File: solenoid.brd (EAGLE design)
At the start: 35.6 x 30.5 mm, 41 parts, among them Y1 ECS-80-S-4X

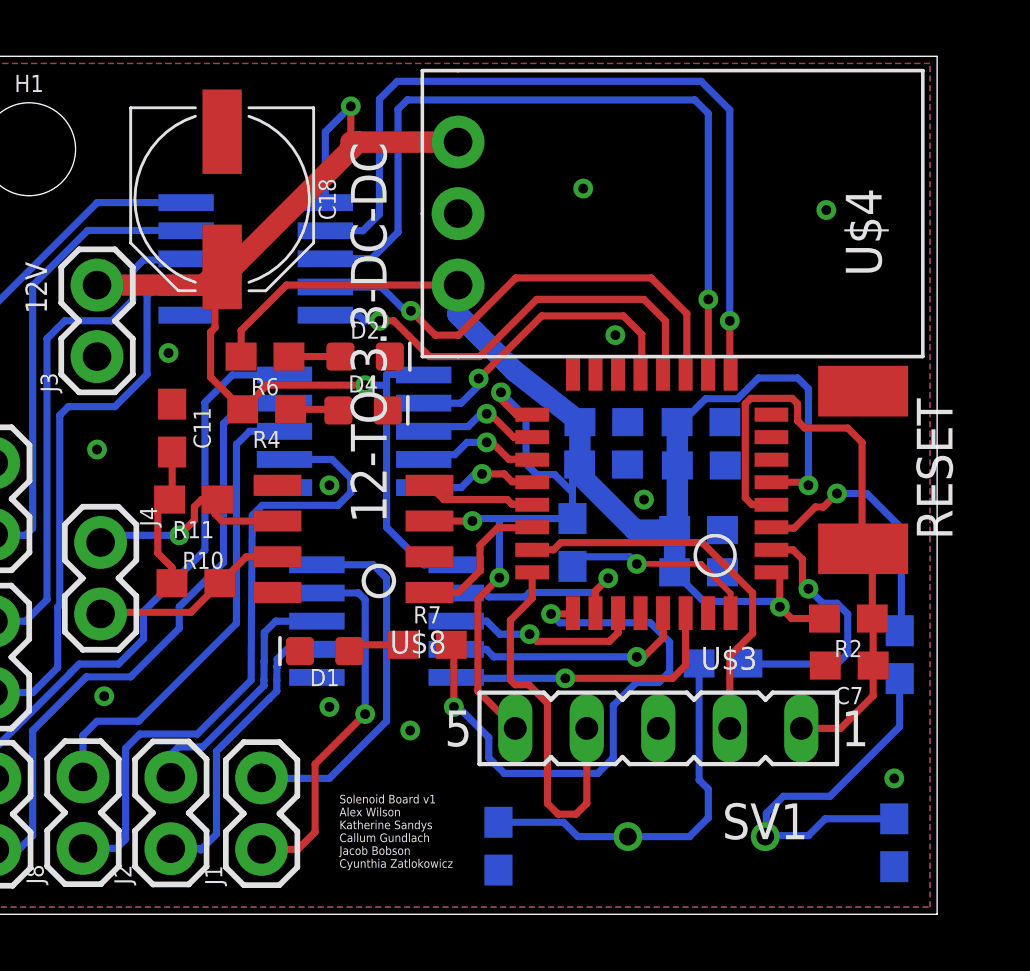
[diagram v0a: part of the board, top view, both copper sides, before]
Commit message: Update 12->3.3 converter, make extra layers inactive, fix names
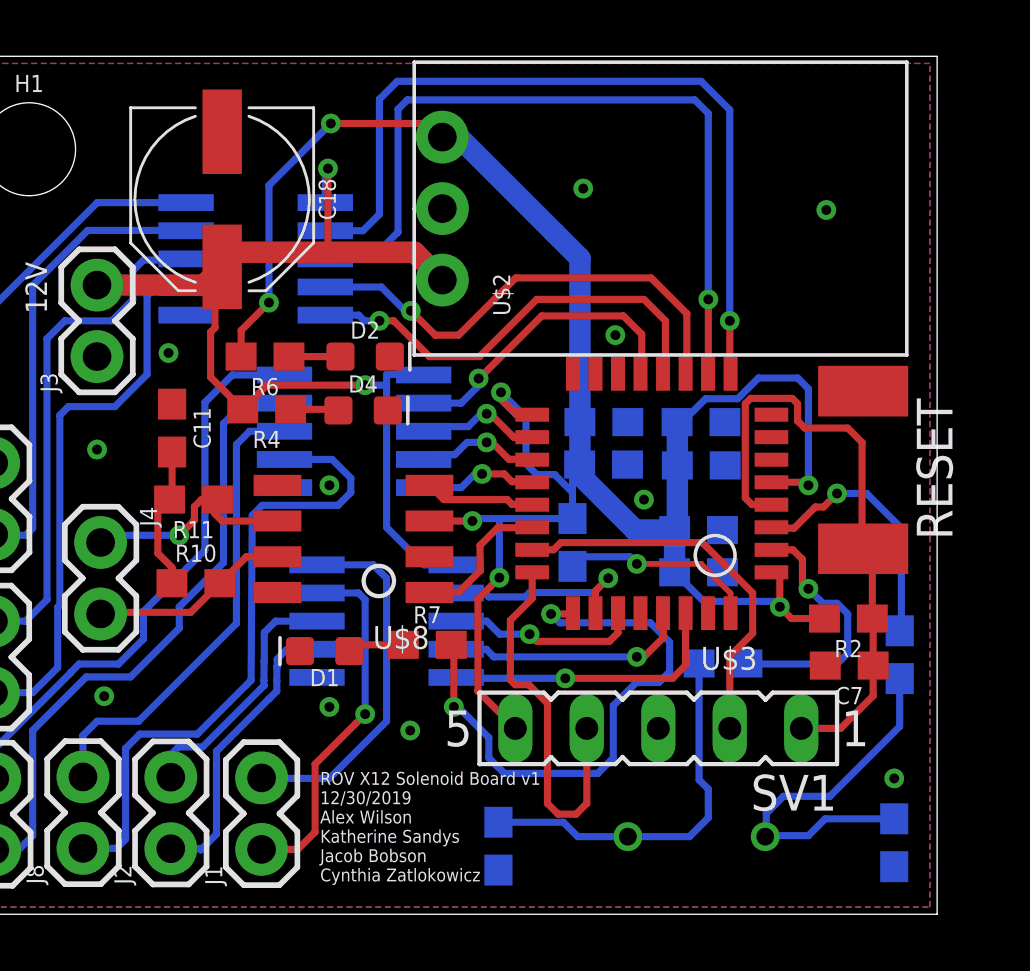
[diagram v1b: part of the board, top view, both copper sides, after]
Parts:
- removed U$4: 12-TO-3.3-DC-DC, ece477:MURATA-DCDC
- added U$2: MURATA-DC-DC, MURATA_3pin_dcdc:MURATA-DC-DC
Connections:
- net +3V3: now also U$2.3; no longer U$4.3.3V
- net 12V: now also U$2.1; no longer U$4.VIN
- net GND: now also U$2.2; no longer U$4.GND
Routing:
- net +3V3: track 67.5 -> 77.6 mm, vias 5 -> 7
- net 12V: track 41.1 -> 38.2 mm
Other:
- board text added: "ROV X12 Solenoid Board v1 12/30/2019 Alex Wilson Katherine Sandys Jacob Bobson Cynthia Zatlokowicz"
- board text removed: "Solenoid Board v1 Alex Wilson Katherine Sandys Callum Gundlach Jacob Bobson Cyunthia Zatlokowicz"

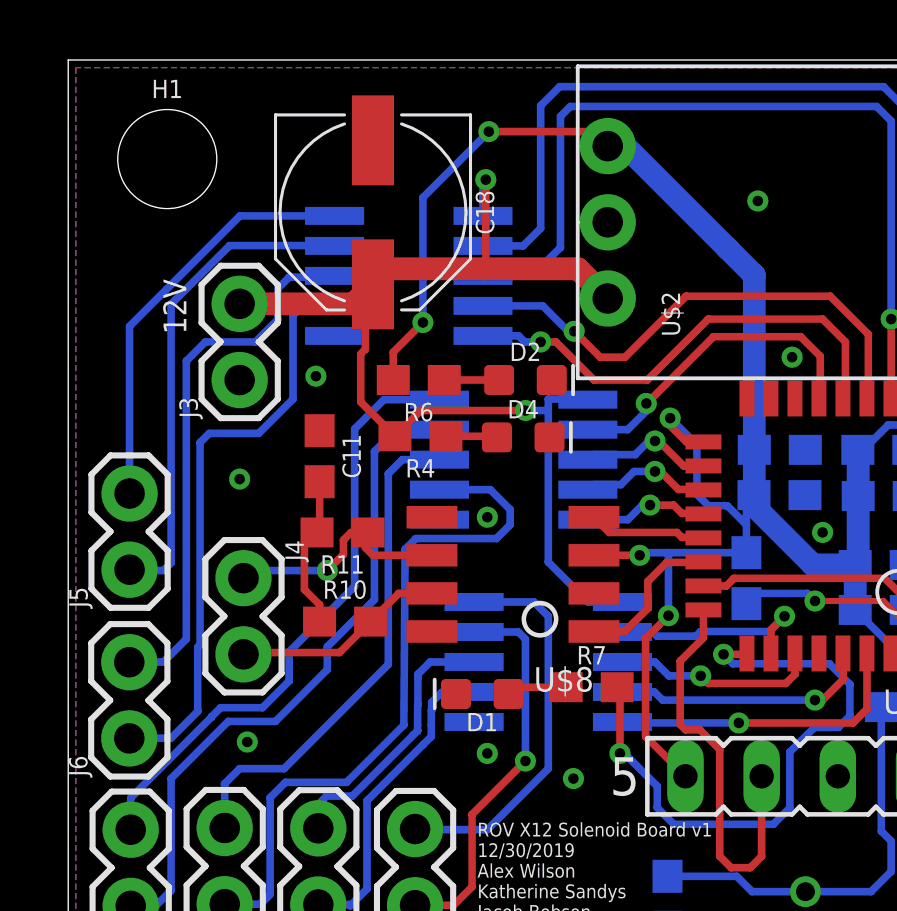
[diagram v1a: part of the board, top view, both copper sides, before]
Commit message: deleted h bridges - broken
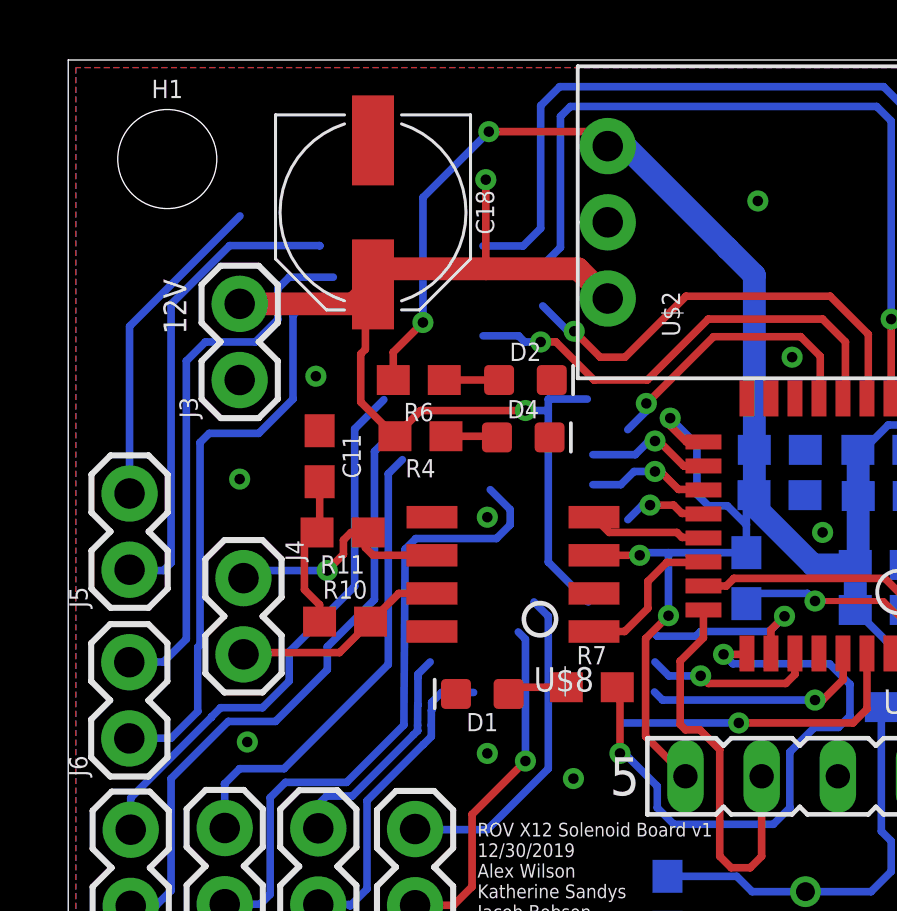
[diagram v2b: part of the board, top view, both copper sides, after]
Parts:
- removed U$1, U$5, U$6: LV8548M, HBridge:SOP100P600X175-10N
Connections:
- net 12V: no longer U$1.VCC, U$5.VCC, U$6.VCC
- net GND: no longer U$1.GND, U$5.GND, U$6.GND
- net GPIO0: no longer U$1.IN4
- net GPIO1: no longer U$1.IN3
- net GPIO10: no longer U$5.IN3
- net GPIO11: no longer U$5.IN4
- net GPIO12: no longer U$6.IN1
- net GPIO13: no longer U$6.IN2
- net GPIO14: no longer U$6.IN3
- net GPIO15: no longer U$6.IN4
- net GPIO2: no longer U$1.IN2
- net GPIO3: no longer U$1.IN1
- net GPIO8: no longer U$5.IN1
- net GPIO9: no longer U$5.IN2
- net SOL1_1: no longer U$1.OUT1
- net SOL1_2: no longer U$1.OUT2
- net SOL2_1: no longer U$1.OUT3
- net SOL2_2: no longer U$1.OUT4
- net SOL3_1: no longer U$5.OUT1
- net SOL3_2: no longer U$5.OUT2
- net SOL4_1: no longer U$5.OUT3
- net SOL4_2: no longer U$5.OUT4
- net SOL5_1: no longer U$6.OUT1
- net SOL5_2: no longer U$6.OUT2
- net SOL6_1: no longer U$6.OUT3
- net SOL6_2: no longer U$6.OUT4
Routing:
- net SOL3_1: track 13.9 -> 10.8 mm
- net 12V: track 38.2 -> 36.0 mm
- net SOL1_1: track 13.0 -> 11.0 mm
- net GPIO10: track 17.1 -> 15.1 mm
- net SOL5_1: track 20.5 -> 18.6 mm
- net SOL6_2: track 23.2 -> 21.5 mm
- net SOL1_2: track 13.0 -> 11.5 mm
- net SOL2_1: track 9.05 -> 7.59 mm
- net SOL5_2: track 22.4 -> 21.0 mm
- net GPIO15: track 4.18 -> 2.84 mm
- net GPIO12: track 10.9 -> 9.54 mm
- net SOL6_1: track 16.8 -> 15.6 mm
- net GPIO2: track 6.87 -> 5.79 mm
- net GPIO1: track 8.62 -> 7.56 mm
- net GPIO3: track 7.16 -> 6.14 mm

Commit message: owo
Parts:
- added U1, U2, U3, U4, U5, U6: QS5K2TR, QS5K2TR:SOT95P280X100-5N
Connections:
- net 12V: now also U1.2, U2.2, U3.2, U4.2, U5.2, U6.2
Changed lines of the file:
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@@
 <attribute name="VALUE" x="21.2852" y="21.2598" size="0.6096" layer="27" font="vector" ratio="20" rot="R90"/>
+</element>
+<element name="U1" library="QS5K2TR" package="SOT95P280X100-5N" value="QS5K2TR" x="-2.3622" y="0.635" smashed="yes">
+<attribute name="AVAILABILITY" value="Good" x="-2.3622" y="0.635" size="1.778" layer="27" display="off"/>
+<attribute name="DESCRIPTION" value=" Mosfet Array 2 N-Channel (Dual) Common Source 30V 2A 1.25W Surface Mount TSMT5 " x="-2.3622" y="0.635" size="1.778" layer="27" display="off"/>
+<attribute name="DIGIKEY-PURCHASE-URL" value="https://snapeda.com/shop?store=DigiKey&amp;id=623744" x="-2.3622" y="0.635" size="1.778" layer="27" display="off"/>
+<attribute name="MF" value="Rohm" x="-2.3622" y="0.635" size="1.778" layer="27" display="off"/>
+<attribute name="MOUSER-PURCHASE-URL" value="https://snapeda.com/shop?store=Mouser&amp;id=623744" x="-2.3622" y="0.635" size="1.778" layer="27" display="off"/>
+<attribute name="MP" value="QS5K2TR" x="-2.3622" y="0.635" size="1.778" layer="27" display="off"/>
+<attribute name="NAME" x="-3.46301875" y="2.436340625" size="0.406703125" layer="25"/>
+<attribute name="PACKAGE" value="SOT-23-5 Rohm" x="-2.3622" y="0.635" size="1.778" layer="27" display="off"/>
+<attribute name="PRICE" value="None" x="-2.3622" y="0.635" size="1.778" layer="27" display="off"/>
+<attribute name="VALUE" x="-3.462309375" y="-1.565209375" size="0.4064375" layer="27"/>
+</element>
+<element name="U2" library="QS5K2TR" package="SOT95P280X100-5N" value="QS5K2TR" x="-7.1628" y="0.635" smashed="yes">
+<attribute name="AVAILABILITY" value="Good" x="-7.1628" y="0.635" size="1.778" layer="27" display="off"/>
+<attribute name="DESCRIPTION" value=" Mosfet Array 2 N-Channel (Dual) Common Source 30V 2A 1.25W Surface Mount TSMT5 " x="-7.1628" y="0.635" size="1.778" layer="27" display="off"/>
+<attribute name="DIGIKEY-PURCHASE-URL" value="https://snapeda.com/shop?store=DigiKey&amp;id=623744" x="-7.1628" y="0.635" size="1.778" layer="27" display="off"/>
+<attribute name="MF" value="Rohm" x="-7.1628" y="0.635" size="1.778" layer="27" display="off"/>
+<attribute name="MOUSER-PURCHASE-URL" value="https://snapeda.com/shop?store=Mouser&amp;id=623744" x="-7.1628" y="0.635" size="1.778" layer="27" display="off"/>
+<attribute name="MP" value="QS5K2TR" x="-7.1628" y="0.635" size="1.778" layer="27" display="off"/>
+<attribute name="NAME" x="-8.26361875" y="2.436340625" size="0.406703125" layer="25"/>
+<attribute name="PACKAGE" value="SOT-23-5 Rohm" x="-7.1628" y="0.635" size="1.778" layer="27" display="off"/>
+<attribute name="PRICE" value="None" x="-7.1628" y="0.635" size="1.778" layer="27" display="off"/>
+<attribute name="VALUE" x="-8.262909375" y="-1.565209375" size="0.4064375" layer="27"/>
+</element>
+<element name="U3" library="QS5K2TR" package="SOT95P280X100-5N" value="QS5K2TR" x="-11.9634" y="0.635" smashed="yes">
+<attribute name="AVAILABILITY" value="Good" x="-11.9634" y="0.635" size="1.778" layer="27" display="off"/>
+<attribute name="DESCRIPTION" value=" Mosfet Array 2 N-Channel (Dual) Common Source 30V 2A 1.25W Surface Mount TSMT5 " x="-11.9634" y="0.635" size="1.778" layer="27" display="off"/>
+<attribute name="DIGIKEY-PURCHASE-URL" value="https://snapeda.com/shop?store=DigiKey&amp;id=623744" x="-11.9634" y="0.635" size="1.778" layer="27" display="off"/>
+<attribute name="MF" value="Rohm" x="-11.9634" y="0.635" size="1.778" layer="27" display="off"/>
+<attribute name="MOUSER-PURCHASE-URL" value="https://snapeda.com/shop?store=Mouser&amp;id=623744" x="-11.9634" y="0.635" size="1.778" layer="27" display="off"/>
+<attribute name="MP" value="QS5K2TR" x="-11.9634" y="0.635" size="1.778" layer="27" display="off"/>
+<attribute name="NAME" x="-13.06421875" y="2.436340625" size="0.406703125" layer="25"/>
+<attribute name="PACKAGE" value="SOT-23-5 Rohm" x="-11.9634" y="0.635" size="1.778" layer="27" display="off"/>
+<attribute name="PRICE" value="None" x="-11.9634" y="0.635" size="1.778" layer="27" display="off"/>
+<attribute name="VALUE" x="-13.063509375" y="-1.565209375" size="0.4064375" layer="27"/>
+</element>
+<element name="U4" library="QS5K2TR" package="SOT95P280X100-5N" value="QS5K2TR" x="-16.764" y="0.635" smashed="yes">
+<attribute name="AVAILABILITY" value="Good" x="-16.764" y="0.635" size="1.778" layer="27" display="off"/>
+<attribute name="DESCRIPTION" value=" Mosfet Array 2 N-Channel (Dual) Common Source 30V 2A 1.25W Surface Mount TSMT5 " x="-16.764" y="0.635" size="1.778" layer="27" display="off"/>
+<attribute name="DIGIKEY-PURCHASE-URL" value="https://snapeda.com/shop?store=DigiKey&amp;id=623744" x="-16.764" y="0.635" size="1.778" layer="27" display="off"/>
+<attribute name="MF" value="Rohm" x="-16.764" y="0.635" size="1.778" layer="27" display="off"/>
+<attribute name="MOUSER-PURCHASE-URL" value="https://snapeda.com/shop?store=Mouser&amp;id=623744" x="-16.764" y="0.635" size="1.778" layer="27" display="off"/>
+<attribute name="MP" value="QS5K2TR" x="-16.764" y="0.635" size="1.778" layer="27" display="off"/>
+<attribute name="NAME" x="-17.86481875" y="2.436340625" size="0.406703125" layer="25"/>
+<attribute name="PACKAGE" value="SOT-23-5 Rohm" x="-16.764" y="0.635" size="1.778" layer="27" display="off"/>
+<attribute name="PRICE" value="None" x="-16.764" y="0.635" size="1.778" layer="27" display="off"/>
+<attribute name="VALUE" x="-17.864109375" y="-1.565209375" size="0.4064375" layer="27"/>
+</element>
+<element name="U5" library="QS5K2TR" package="SOT95P280X100-5N" value="QS5K2TR" x="-21.5646" y="0.635" smashed="yes">
+<attribute name="AVAILABILITY" value="Good" x="-21.5646" y="0.635" size="1.778" layer="27" display="off"/>
+<attribute name="DESCRIPTION" value=" Mosfet Array 2 N-Channel (Dual) Common Source 30V 2A 1.25W Surface Mount TSMT5 " x="-21.5646" y="0.635" size="1.778" layer="27" display="off"/>
+<attribute name="DIGIKEY-PURCHASE-URL" value="https://snapeda.com/shop?store=DigiKey&amp;id=623744" x="-21.5646" y="0.635" size="1.778" layer="27" display="off"/>
+<attribute name="MF" value="Rohm" x="-21.5646" y="0.635" size="1.778" layer="27" display="off"/>
+<attribute name="MOUSER-PURCHASE-URL" value="https://snapeda.com/shop?store=Mouser&amp;id=623744" x="-21.5646" y="0.635" size="1.778" layer="27" display="off"/>
+<attribute name="MP" value="QS5K2TR" x="-21.5646" y="0.635" size="1.778" layer="27" display="off"/>
+<attribute name="NAME" x="-22.66541875" y="2.436340625" size="0.406703125" layer="25"/>
+<attribute name="PACKAGE" value="SOT-23-5 Rohm" x="-21.5646" y="0.635" size="1.778" layer="27" display="off"/>
+<attribute name="PRICE" value="None" x="-21.5646" y="0.635" size="1.778" layer="27" display="off"/>
+<attribute name="VALUE" x="-22.664709375" y="-1.565209375" size="0.4064375" layer="27"/>
+</element>
+<element name="U6" library="QS5K2TR" package="SOT95P280X100-5N" value="QS5K2TR" x="-26.3652" y="0.635" smashed="yes">
+<attribute name="AVAILABILITY" value="Good" x="-26.3652" y="0.635" size="1.778" layer="27" display="off"/>
+<attribute name="DESCRIPTION" value=" Mosfet Array 2 N-Channel (Dual) Common Source 30V 2A 1.25W Surface Mount TSMT5 " x="-26.3652" y="0.635" size="1.778" layer="27" display="off"/>
+<attribute name="DIGIKEY-PURCHASE-URL" value="https://snapeda.com/shop?store=DigiKey&amp;id=623744" x="-26.3652" y="0.635" size="1.778" layer="27" display="off"/>
+<attribute name="MF" value="Rohm" x="-26.3652" y="0.635" size="1.778" layer="27" display="off"/>
+<attribute name="MOUSER-PURCHASE-URL" value="https://snapeda.com/shop?store=Mouser&amp;id=623744" x="-26.3652" y="0.635" size="1.778" layer="27" display="off"/>
+<attribute name="MP" value="QS5K2TR" x="-26.3652" y="0.635" size="1.778" layer="27" display="off"/>
+<attribute name="NAME" x="-27.46601875" y="2.436340625" size="0.406703125" layer="25"/>
+<attribute name="PACKAGE" value="SOT-23-5 Rohm" x="-26.3652" y="0.635" size="1.778" layer="27" display="off"/>
+<attribute name="PRICE" value="None" x="-26.3652" y="0.635" size="1.778" layer="27" display="off"/>
+<attribute name="VALUE" x="-27.465309375" y="-1.565209375" size="0.4064375" layer="27"/>
 </element>
 </elements>
@@
 <wire x1="13.9192" y1="26.4922" x2="13.9192" y2="23.5204" width="0.254" layer="1"/>
 <wire x1="16.9926" y1="23.5204" x2="13.9192" y2="23.5204" width="0.762" layer="1"/>
+<contactref element="U1" pad="2"/>
+<contactref element="U2" pad="2"/>
+<contactref element="U3" pad="2"/>
+<contactref element="U4" pad="2"/>
+<contactref element="U5" pad="2"/>
+<contactref element="U6" pad="2"/>
+<wire x1="-3.5072" y1="0.635" x2="10.892" y2="17.938" width="0" layer="19" extent="1-1"/>
+<wire x1="-8.3078" y1="0.635" x2="-3.5072" y2="0.635" width="0" layer="19" extent="1-1"/>
+<wire x1="-13.1084" y1="0.635" x2="-8.3078" y2="0.635" width="0" layer="19" extent="1-1"/>
+<wire x1="-17.909" y1="0.635" x2="-13.1084" y2="0.635" width="0" layer="19" extent="1-1"/>
+<wire x1="-22.7096" y1="0.635" x2="-17.909" y2="0.635" width="0" layer="19" extent="1-1"/>
+<wire x1="-27.5102" y1="0.635" x2="-22.7096" y2="0.635" width="0" layer="19" extent="1-1"/>
 </signal>
 <signal name="N$25">

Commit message: potentially finished schematic
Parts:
- moved U6 36.9 mm to (7.24, -14.7)
- moved U5 28.5 mm to (2.44, -14.7)
- moved U4 26.1 mm to (7.24, -9.58)
- moved U3 17.7 mm to (2.44, -9.58)
- moved U2 15.3 mm to (7.24, -4.47)
- moved U1 7.01 mm to (2.44, -4.47)
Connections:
- new net SOLI1_1: U1.5
- new net SOLI1_2: U1.4
- net GPIO0: now also U2.3
- net GPIO1: now also U2.1
- net GPIO10: now also U4.1
- net GPIO11: now also U4.3
- net GPIO12: now also U5.1
- net GPIO13: now also U5.3
- net GPIO14: now also U6.1
- net GPIO15: now also U6.3
- net GPIO2: now also U1.3
- net GPIO3: now also U1.1
- net GPIO8: now also U3.1
- net GPIO9: now also U3.3
- net SOL2_1: now also U2.5
- net SOL2_2: now also U2.4
- net SOL3_1: now also U3.5
- net SOL3_2: now also U3.4
- net SOL4_1: now also U4.5
- net SOL4_2: now also U4.4
- net SOL5_1: now also U5.5
- net SOL5_2: now also U5.4
- net SOL6_1: now also U6.5
- net SOL6_2: now also U6.4

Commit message: solenoid work
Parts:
- removed U3, U4, U5, U6: QS5K2TR, QS5K2TR:SOT95P280X100-5N
- U1, U2: value QS5K2TR -> ULN2003V12; device QS5K2TR:SOT95P280X100-5N -> ULN2003V12:ULN2003V12
- moved U1 25.9 mm to (21.6, 13.0), flipped to the bottom, turned to 270 degrees
- moved R7 23.7 mm to (11.9, -13.5)
- moved C11 23.4 mm to (3.05, -5.51)
- moved D1 23.4 mm to (8.47, -13.4)
- moved D4 23.4 mm to (9.83, -4.88)
- moved R11 23.4 mm to (3.81, -8.05)
- moved R4 23.4 mm to (6.41, -4.85)
- moved R6 23.4 mm to (6.35, -2.97)
- moved D2 23.3 mm to (9.91, -2.87)
- moved R10 23.2 mm to (3.74, -10.8)
- moved U2 22.5 mm to (11.5, 17.6), flipped to the bottom
- moved C8 14.1 mm to (34.0, 2.92), turned to 90 degrees
- moved C10 10.8 mm to (33.3, 14.8), turned to 180 degrees
- moved C2 9.60 mm to (33.2, 18.7)
- moved C4 9.59 mm to (33.3, 16.8)
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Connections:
- removed net SOLI1_1: U1.5
- removed net SOLI1_2: U1.4
- net 12V: now also U1.9, U2.9; no longer U1.2, U2.2, U3.2, U4.2, U5.2, U6.2
- net GND: now also U1.8, U2.8
- net GPIO0: now also U1.6; no longer U2.3
- net GPIO1: now also U1.5; no longer U2.1
- net GPIO10: now also U2.3; no longer U4.1
- net GPIO11: now also U2.4; no longer U4.3
- net GPIO12: now also U2.5; no longer U5.1
- net GPIO13: now also U2.6; no longer U5.3
- net GPIO14: now also U1.1; no longer U6.1
- net GPIO15: now also U1.2; no longer U6.3
- net GPIO2: now also U1.4; no longer U1.3
- net GPIO3: now also U1.3; no longer U1.1
- net GPIO8: now also U2.1; no longer U3.1
- net GPIO9: now also U2.2; no longer U3.3
- net SOL1_1: now also U1.14
- net SOL1_2: now also U1.13
- net SOL2_1: now also U1.12; no longer U2.5
- net SOL2_2: now also U1.11; no longer U2.4
- net SOL3_1: now also U2.16; no longer U3.5
- net SOL3_2: now also U2.15; no longer U3.4
- net SOL4_1: now also U2.14; no longer U4.5
- net SOL4_2: now also U2.13; no longer U4.4
- net SOL5_1: now also U2.12; no longer U5.5
- net SOL5_2: now also U2.11; no longer U5.4
- net SOL6_1: now also U1.16; no longer U6.5
- net SOL6_2: now also U1.15; no longer U6.4
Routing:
- net +3V3: track 77.6 -> 19.4 mm, vias 7 -> 1
- net 12V: track 36.0 -> 0.00 mm, vias 2 -> 0
- net GPIO8: track 28.8 -> 0.00 mm, vias 1 -> 0
- net GPIO9: track 27.9 -> 0.00 mm, vias 1 -> 0
- net SOL6_2: track 21.5 -> 0.00 mm
- net SOL5_2: track 21.0 -> 0.00 mm
- net LED: track 20.4 -> 0.00 mm, vias 2 -> 0
- net SOL4_2: track 19.6 -> 0.00 mm
- net SOL5_1: track 18.6 -> 0.00 mm
- net SOL4_1: track 18.2 -> 0.00 mm
- net SOL3_2: track 15.9 -> 0.00 mm
- net GPIO11: track 15.8 -> 0.00 mm, vias 1 -> 0
- net SOL6_1: track 15.6 -> 0.00 mm
- net GPIO10: track 15.1 -> 0.00 mm, vias 1 -> 0
- net SWDIO: track 13.8 -> 0.00 mm
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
